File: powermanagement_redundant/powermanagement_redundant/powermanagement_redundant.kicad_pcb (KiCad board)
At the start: 2 copper layers, 40 parts, among them SW1 SW_DIP_x01, SW2 SW_DIP_x01

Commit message: PCB angefangen
PCB halt angefangen
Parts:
- added J2: Screw_Terminal_01x01, MountingHole:MountingHole_3.2mm_M3_Pad_Via, F.Cu at (115.0, 24.2)
- added J3: Screw_Terminal_01x01, MountingHole:MountingHole_3.2mm_M3_Pad_Via, F.Cu at (98.5, 24.2)
- added J4: Screw_Terminal_01x01, MountingHole:MountingHole_3.2mm_M3_Pad_Via, F.Cu at (35.0, 24.2)
- added J5: Screw_Terminal_01x01, MountingHole:MountingHole_3.2mm_M3_Pad_Via, F.Cu at (60.0, 24.2)
- added J6: Screw_Terminal_01x01, MountingHole:MountingHole_3.2mm_M3_Pad_Via, F.Cu at (51.5, 24.2)
- added J7: Screw_Terminal_01x01, MountingHole:MountingHole_3.2mm_M3_Pad_Via, F.Cu at (43.5, 24.2)
- added J8: Screw_Terminal_01x01, MountingHole:MountingHole_3.2mm_M3_Pad_Via, F.Cu at (90.0, 24.2)
- added Jp: Screw_Terminal_01x01, MountingHole:MountingHole_3.2mm_M3_Pad_Via, F.Cu at (106.5, 24.2)
- moved R_{SENSEB}1 76.2 mm to (50.8, 31.3), turned to 90 degrees
- moved D_{InB}1 73.0 mm to (50.8, 39.5), turned to 180 degrees
- moved K_{B}1 69.5 mm to (54.9, 31.1), turned to 90 degrees
- moved SW2 68.9 mm to (43.2, 38.1), turned to 180 degrees
- moved C5 61.6 mm to (64.0, 44.7)
- moved R_{MON}1 59.3 mm to (81.3, 48.3)
- moved D1 58.4 mm to (121.9, 35.6), turned to -90 degrees
- moved R7 48.3 mm to (171.1, 47.5)
- moved C1 48.3 mm to (149.6, 57.6)
- moved C6 48.3 mm to (156.7, 50.1)
- moved C_{INA}1 48.3 mm to (161.5, 48.3)
- moved R1 48.3 mm to (163.9, 54.2)
- moved R_{G2A}1 48.3 mm to (166.3, 48.2)
- moved R_{SETB}1 48.3 mm to (159.2, 53.1)
- moved C2 48.3 mm to (149.6, 54.6)
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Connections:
- net GND1 renamed GND
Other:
- board outline added: 110 x 17.5 mm

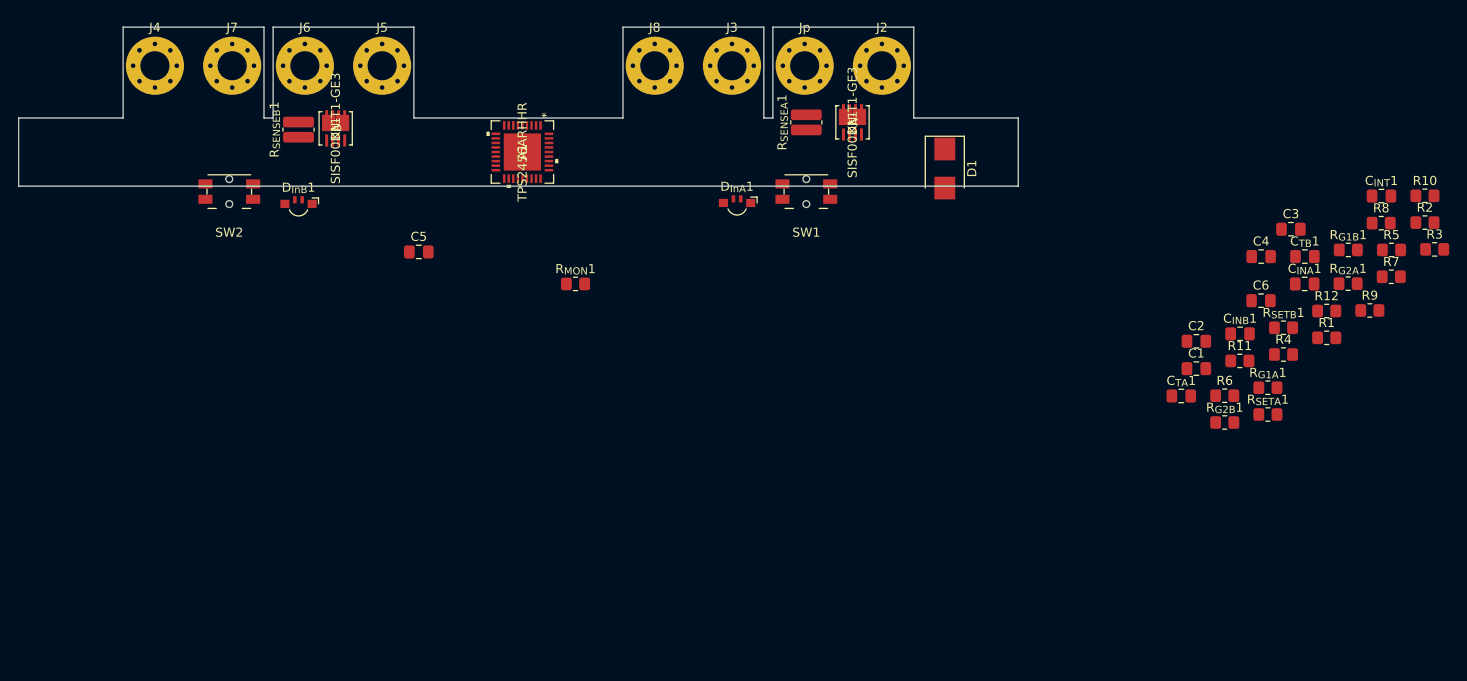
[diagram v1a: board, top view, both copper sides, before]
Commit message: Alle komponenten auf der Platine Platziert
Alles passt iwie ist aber knapp.
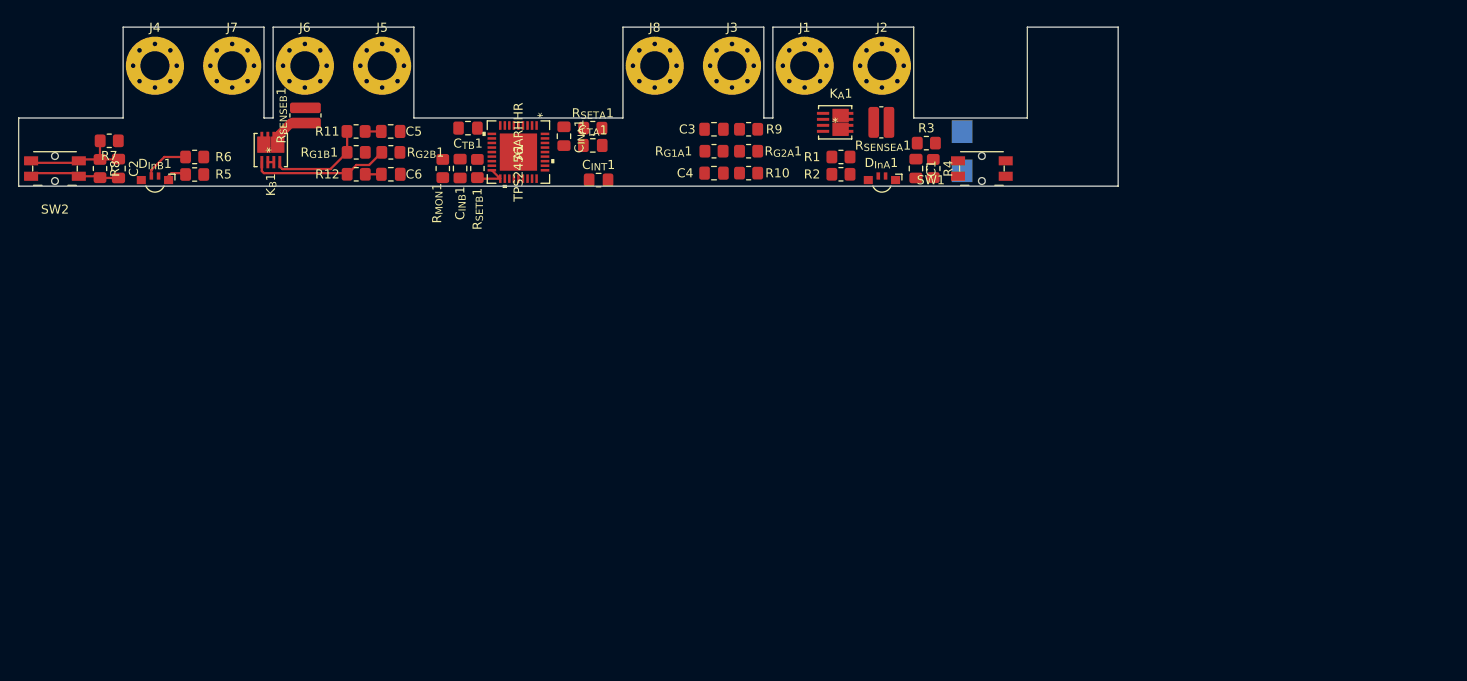
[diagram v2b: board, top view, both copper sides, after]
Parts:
- D1: moved to B.Cu
- moved R7 141.9 mm to (30.0, 32.5), turned to 180 degrees
- moved R8 141.1 mm to (29.0, 35.6), turned to -90 degrees
- moved R5 132.0 mm to (39.4, 36.2)
- moved C2 120.1 mm to (31.0, 35.6), turned to -90 degrees
- moved R6 116.4 mm to (39.4, 34.3)
- moved R_{G1B}1 109.7 mm to (57.1, 33.8), turned to 180 degrees
- moved R12 107.8 mm to (57.1, 36.2), turned to 180 degrees
- moved R11 100.5 mm to (57.1, 31.5), turned to 180 degrees
- moved C6 96.8 mm to (61.0, 36.2)
- moved R_{G2B}1 96.5 mm to (61.0, 33.8), turned to 180 degrees
- moved C_{TB}1 93.2 mm to (69.4, 31.1), turned to 180 degrees
- moved R_{SETB}1 90.4 mm to (70.5, 35.6), turned to -90 degrees
- moved C_{INB}1 87.7 mm to (68.6, 35.6), turned to -90 degrees
- moved C_{INT}1 86.2 mm to (83.8, 36.8)
- moved C_{INA}1 83.1 mm to (80.0, 32.0), turned to -90 degrees
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- renumbered Jp to J1
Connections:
- A1 pad 17: SETA -> SETBB
- K_{A}1 pad 7: Net-(K_{A}1-Pad7) -> SENMA
- K_{A}1 pad 8: Net-(K_{A}1-Pad7) -> SENMA
- K_{B}1 pad 1: Net-(K_{B}1-Pad1) -> Net-(R12-Pad2)
- K_{B}1 pad 5: LOAD -> SENMB
- K_{B}1 pad 6: LOAD -> SENMB
- K_{B}1 pad 7: Net-(K_{B}1-Pad7) -> LOAD
- K_{B}1 pad 8: Net-(K_{B}1-Pad7) -> LOAD
- R11 pad 2: Net-(K_{B}1-Pad1) -> Net-(K_{B}1-Pad4)
- R12 pad 2: Net-(K_{B}1-Pad4) -> Net-(R12-Pad2)
- R_{G1B}1 pad 2: Net-(K_{B}1-Pad1) -> Net-(K_{B}1-Pad4)
- R_{G2B}1 pad 2: Net-(K_{B}1-Pad4) -> Net-(R12-Pad2)
- R_{SENSEA}1 pad 1: Net-(K_{A}1-Pad7) -> SENMA
- R_{SENSEB}1 pad 1: Net-(K_{B}1-Pad7) -> SENMB
- R_{SETB}1 pad 1: SETA -> SETBB
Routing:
- net Net-(R12-Pad2): track 0.00 -> 15.3 mm
- net ENB: track 0.00 -> 11.9 mm
- net Net-(K_{B}1-Pad4): track 0.00 -> 11.1 mm
- net GND: track 0.00 -> 10.0 mm
- net Net-(D_{InB}1-Pad3): track 0.00 -> 5.02 mm
- net SENMB: track 0.00 -> 4.16 mm
- net INB: track 0.00 -> 3.87 mm
- net Net-(D_{InB}1-Pad1): track 0.00 -> 2.50 mm
- net Net-(C6-Pad1): track 0.00 -> 1.77 mm
- net Net-(C5-Pad1): track 0.00 -> 1.77 mm
- net Net-(K_{B}1-Pad2): track 0.00 -> 0.66 mm
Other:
- board size 110 x 17.5 mm -> 121 x 17.5 mm
- copper layers 2 -> 4
